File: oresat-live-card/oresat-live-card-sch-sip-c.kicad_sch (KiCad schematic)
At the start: 32 parts, among them J7 DM3BT-DSF-PEJS, U11 TCAN330G, U3 THGBMJG7C2LBAU8, U7 OSD3358-512M-BSM

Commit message: Updated SIP A, B, and C. Lots of cleanup of crazy routing - this board is long in the tooth and has been rerouted several times, so there's a lot of crazy routing. Cleaning up a bit is really helping.
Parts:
- removed R97: 0, Resistor_SMD:R_0603_1608Metric, symbol oresat-passives:R-US
- removed TP22, TP35: TEST-POINT3X4, oresat-misc:TestPoint_Pad_D1.0mm, symbol oresat-misc:Test-Point-1mm-round
- U11: symbol oresat-ics:TCAN330 -> Interface_CAN_LIN:TCAN330
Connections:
- net +3.3V: now also C2.1, C5.1, C6.1, C78.1, C9.1, U3.C6 (VDDQ), U3.E6 (VDDIO), U3.F5 (VDDIO), U3.J10 (VDDIO), U3.K9 (VDDIO), U3.M4 (VDDQ), U3.N4 (VDDQ), U3.P3 (VDDQ), U3.P5 (VDDQ)
- net GND: no longer U11.8 (S)
- net CAN1_TXD: now reaches U11.1 (TXD), U7.A11 (UART1_RXD)
- net CAN1_RXD: now reaches U11.4 (RXD), U7.B11 (UART1_TXD)
- no-connect marks 47 -> 49
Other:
- note added: "S and SHDN have internal pulldowns."
- note added: "SD CARD"
- note added: "USER LEDs"
- note added: "eMMC"
- note removed: "NOTE: All these signals are outputs with the exception of FLASH. Likewise, I put the outputs on GPIO2,3 and inputs on GPIO0. I am not sure if this is better, but it seemed logical"
- note removed: "S and SHDN have internal pulldown."
- note removed: "SD Card Circuit pinout from RED board"
- note removed: "These capacitor values have varied slightly in the different designs I have looked at, but these values should be fine"
- note removed: "USR LEDs"
- note removed: "eMMC Circuit"
- moved on the sheet: C11, C31, C8, D2, D3, D4, D5, J7, R2, R3, R4, R5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

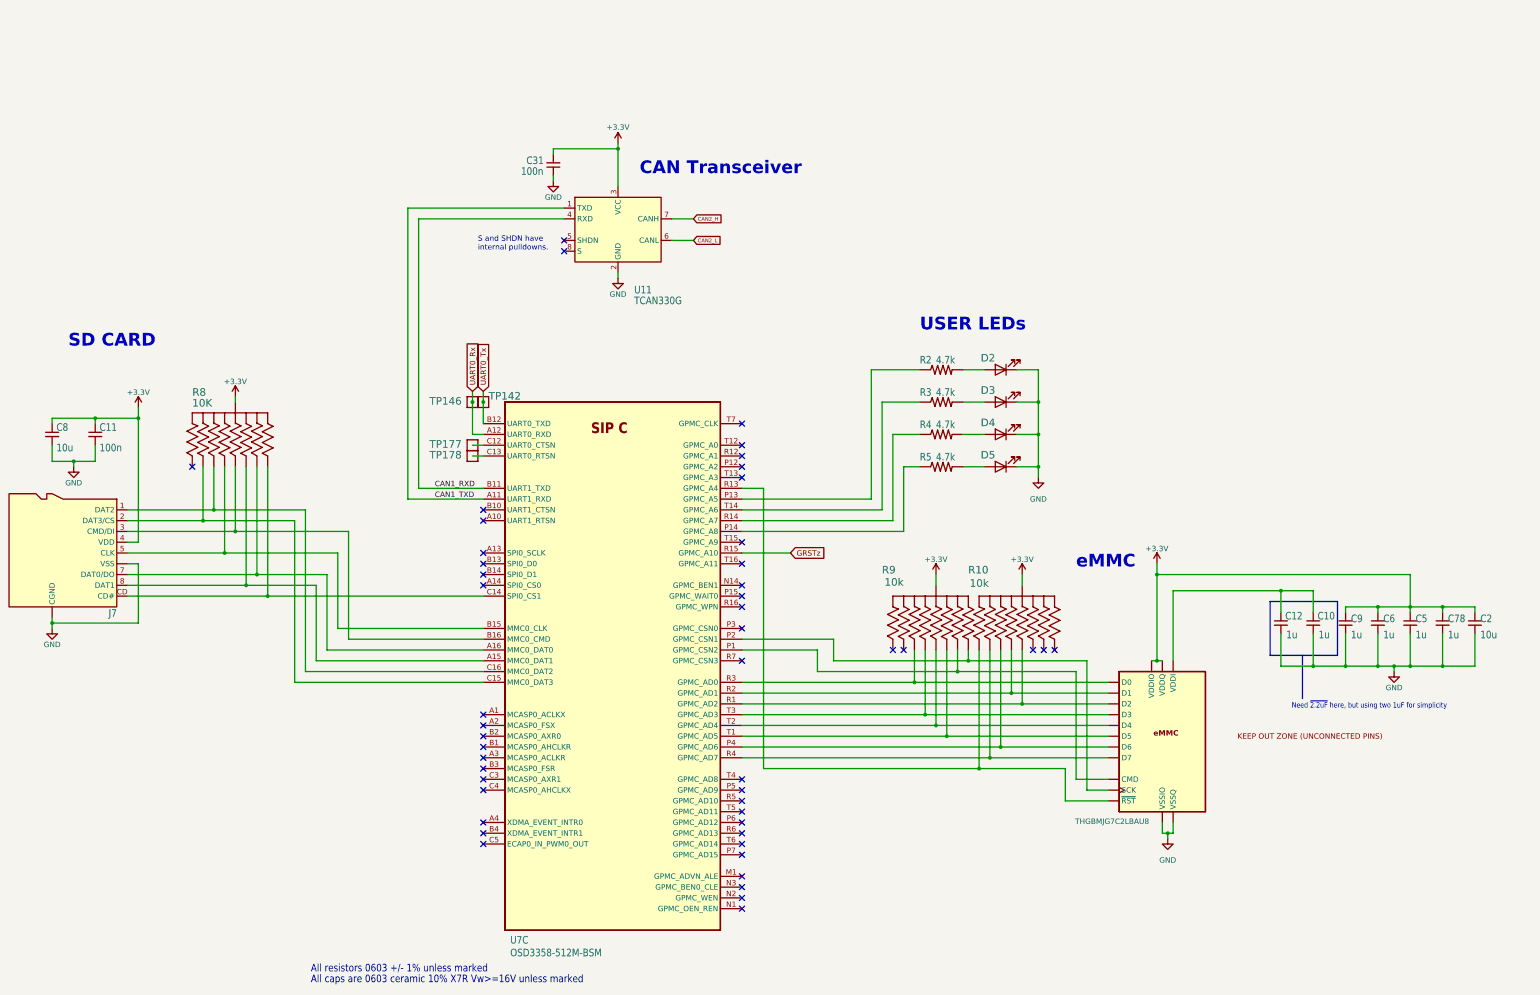
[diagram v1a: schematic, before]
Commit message: Schematic cleaned up and should be good to go. Lots of DRC errors to fix. Also waiting for design review.
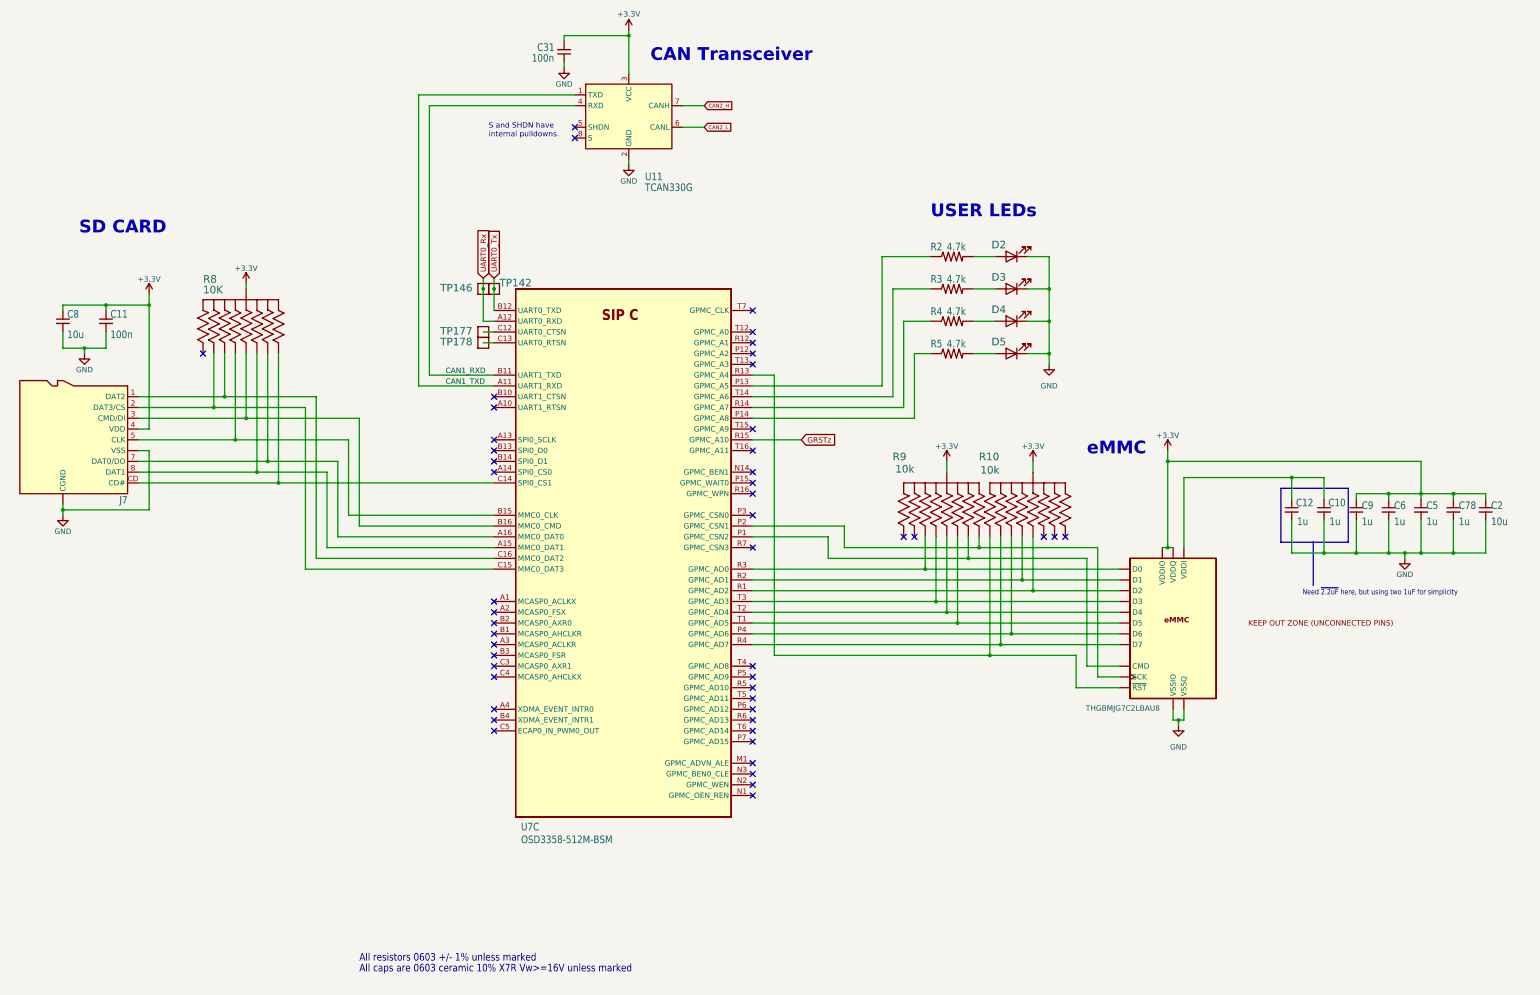
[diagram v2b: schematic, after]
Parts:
- J7: footprint oresat-live-card:DM3BT-DSF-PEJS -> oresat-connectors:J-Hirose-DM3BT-DSF-PEJS
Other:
- moved on the sheet: C10, C11, C12, C2, C31, C5, C6, C78, C8, C9, D2, D3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

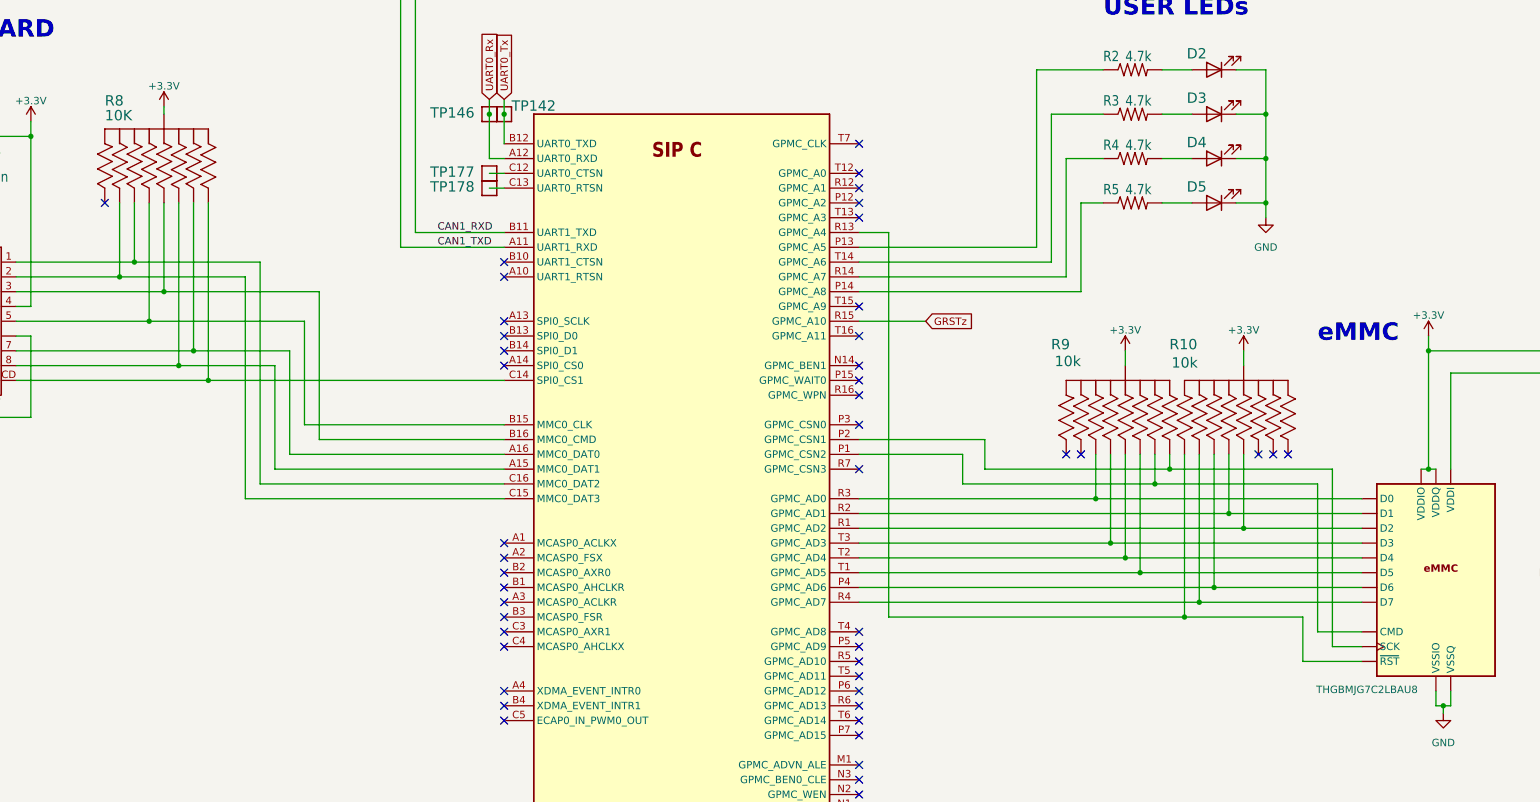
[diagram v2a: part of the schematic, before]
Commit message: added Olivers BOM and footprint changes, cleaned up pcb
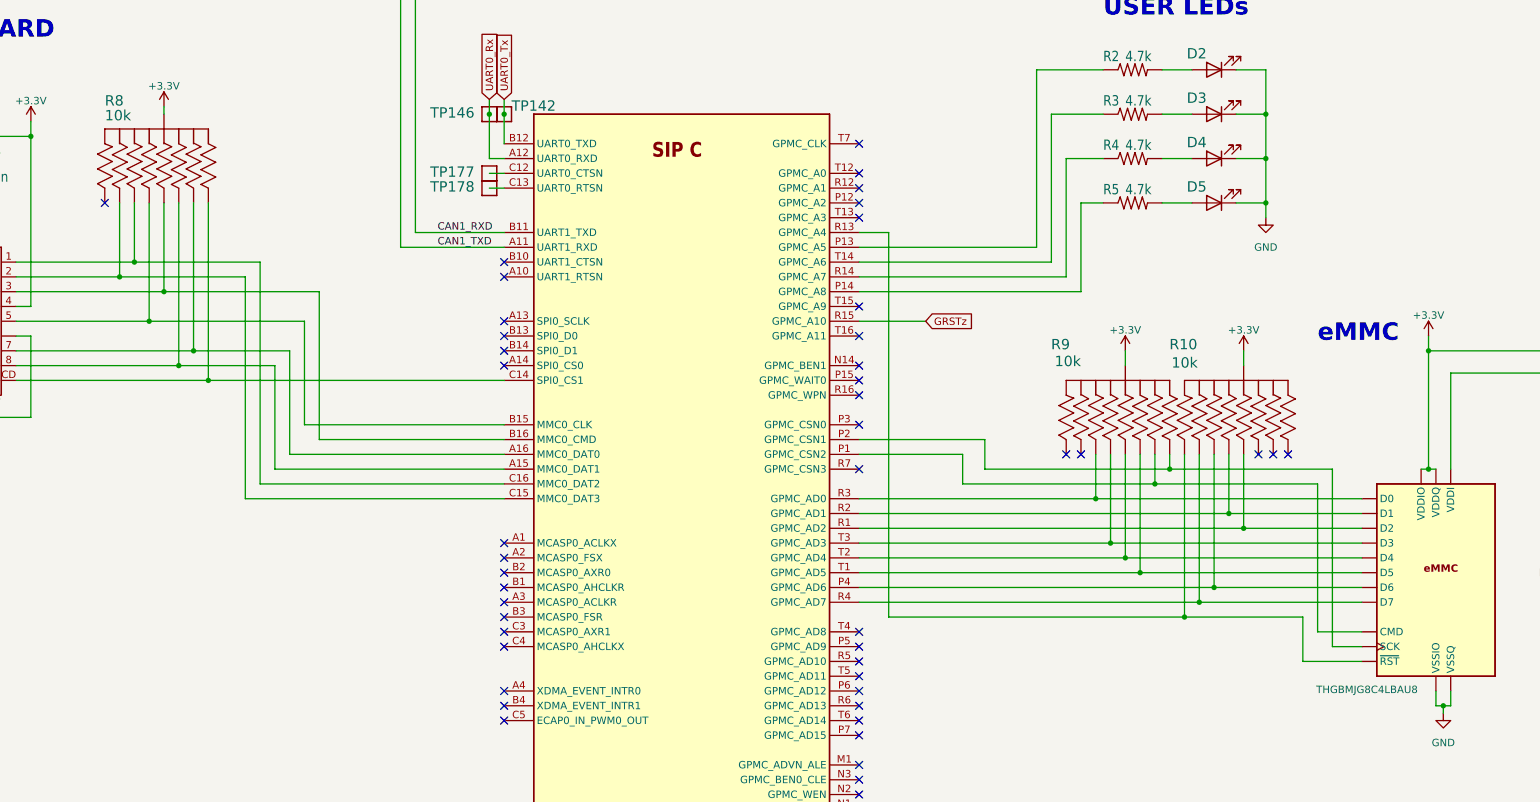
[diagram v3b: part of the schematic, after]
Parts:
- C10, C11, C12, C31, C5, C6, C78, C9, R2, R3, R4, R5: footprint Resistor_SMD:R_0603_1608Metric -> oresat-passives:0603-C
- C2, C8: footprint Resistor_SMD:R_0805_2012Metric -> oresat-passives:0805-C
- R8: value 10K -> 10k
- U3: value THGBMJG7C2LBAU8 -> THGBMJG8C4LBAU8; DIS (none) -> Mouser; DPN 757-THGBMJG7C2LBAU8 -> 757-THGBMJG8C4LBAU8; MPN THGBMJG7C2LBAU8 -> THGBMJG8C4LBAU8
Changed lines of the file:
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@@
 			)
 		)
-		(property "Footprint" "Resistor_SMD:R_0603_1608Metric"
+		(property "Footprint" "oresat-passives:0603-C"
 			(at 353.06 154.94 0)
 			(effects
@@
 			)
 		)
-		(property "Footprint" "Resistor_SMD:R_0603_1608Metric"
+		(property "Footprint" "oresat-passives:0603-C"
 			(at 375.92 154.94 0)
 			(effects
@@
 			)
 		)
-		(property "Footprint" "Resistor_SMD:R_0603_1608Metric"
+		(property "Footprint" "oresat-passives:0603-C"
 			(at 265.43 118.11 0)
 			(effects
@@
 			)
 		)
-		(property "Footprint" "Resistor_SMD:R_0603_1608Metric"
+		(property "Footprint" "oresat-passives:0603-C"
 			(at 360.68 154.94 0)
 			(effects
@@
 			)
 		)
-		(property "Footprint" "Resistor_SMD:R_0603_1608Metric"
+		(property "Footprint" "oresat-passives:0603-C"
 			(at 383.54 154.94 0)
 			(effects
@@
 			)
 		)
-		(property "Footprint" "Resistor_SMD:R_0603_1608Metric"
+		(property "Footprint" "oresat-passives:0603-C"
 			(at 265.43 95.25 0)
 			(effects
@@
 			)
 		)
-		(property "Value" "10K"
+		(property "Value" "10k"
 			(at 88.9 104.14 90)
 			(effects
@@
 			)
 		)
-		(property "Footprint" "Resistor_SMD:R_0805_2012Metric"
+		(property "Footprint" "oresat-passives:0805-C"
 			(at 55.88 110.49 0)
 			(effects
@@
 			)
 		)
-		(property "Footprint" "Resistor_SMD:R_0603_1608Metric"
+		(property "Footprint" "oresat-passives:0603-C"
 			(at 265.43 102.87 0)
 			(effects
@@
 			)
 		)
-		(property "Footprint" "Resistor_SMD:R_0603_1608Metric"
+		(property "Footprint" "oresat-passives:0603-C"
 			(at 345.44 154.94 0)
 			(effects
@@
 			)
 		)
-		(property "Footprint" "Resistor_SMD:R_0603_1608Metric"
+		(property "Footprint" "oresat-passives:0603-C"
 			(at 265.43 110.49 0)
 			(effects
@@
 			)
 		)
-		(property "Footprint" "Resistor_SMD:R_0603_1608Metric"
+		(property "Footprint" "oresat-passives:0603-C"
 			(at 368.3 154.94 0)
 			(effects
@@
 			)
 		)
-		(property "Footprint" "Resistor_SMD:R_0603_1608Metric"
+		(property "Footprint" "oresat-passives:0603-C"
 			(at 66.04 110.49 0)
 			(effects
@@
 			)
 		)
-		(property "Footprint" "Resistor_SMD:R_0603_1608Metric"
+		(property "Footprint" "oresat-passives:0603-C"
 			(at 173.99 46.99 0)
 			(effects
@@
 			)
 		)
-		(property "Value" "THGBMJG7C2LBAU8"
+		(property "Value" "THGBMJG8C4LBAU8"
 			(at 296.926 202.438 0)
 			(effects
@@
 			)
 		)
-		(property "Description" "IC FLASH 16GB EMMC 153FBGA"
+		(property "Description" "IC FLASH 32GB EMMC 153FBGA"
 			(at 317.5 181.61 0)
 			(effects
@@
 			)
 		)
-		(property "MPN" "THGBMJG7C2LBAU8"
+		(property "MPN" " THGBMJG8C4LBAU8"
 			(at 317.5 181.61 0)
 			(effects
@@
 			)
 		)
-		(property "DPN" "757-THGBMJG7C2LBAU8"
+		(property "DPN" "757-THGBMJG8C4LBAU8"
 			(at 317.5 181.61 0)
 			(effects
@@
 			)
 		)
-		(property "DIS" ""
+		(property "DIS" "Mouser"
 			(at 317.5 181.61 0)
 			(effects
@@
 			)
 		)
-		(property "Footprint" "Resistor_SMD:R_0805_2012Metric"
+		(property "Footprint" "oresat-passives:0805-C"
 			(at 391.16 154.94 0)
 			(effects

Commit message: added 100p cap to U34 CTRL line, some BOM changes
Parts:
- R2, R3, R4, R5: DPN ERJ-3EKF4701V -> P4.70KHCT-ND
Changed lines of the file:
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@@
 			)
 		)
-		(property "DPN" "ERJ-3EKF4701V"
+		(property "DPN" "P4.70KHCT-ND"
 			(at 265.43 118.11 0)
 			(effects
@@
 			)
 		)
-		(property "DPN" "ERJ-3EKF4701V"
+		(property "DPN" "P4.70KHCT-ND"
 			(at 265.43 95.25 0)
 			(effects
@@
 			)
 		)
-		(property "DPN" "ERJ-3EKF4701V"
+		(property "DPN" "P4.70KHCT-ND"
 			(at 265.43 102.87 0)
 			(effects
@@
 			)
 		)
-		(property "DPN" "ERJ-3EKF4701V"
+		(property "DPN" "P4.70KHCT-ND"
 			(at 265.43 110.49 0)
 			(effects

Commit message: Components Update
Changed Debug connector and performed minor rerouting
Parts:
- TP142, TP146: footprint oresat-misc:TestPoint_Pad_D1.0mm -> oresat-misc:TestPoint-0.75mm-th
